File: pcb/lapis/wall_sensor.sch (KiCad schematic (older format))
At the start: 0 parts

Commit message: 基板修正途中　ソフト動作確認まで
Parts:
- added Q4: LTR-4206E, LED_THT:LED_D3.0mm_Horizontal_O1.27mm_Z2.0mm_IRBlack, symbol Device:Q_Photo_NPN
- added R5: 1k, Resistor_SMD:R_0201_0603Metric_Pad0.64x0.40mm_HandSolder, symbol Device:R
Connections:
- new net +3V3: Q4.1 (C)
- new net GND: R5.2
- new net WALLSENSOR_ADC: Q4.2 (E), R5.1
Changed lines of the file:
@@
 $Descr A4 11693 8268
 encoding utf-8
-Sheet 1 14
+Sheet 5 14
 Title ""
 Date ""
@@
 Comment4 ""
 $EndDescr
+$Comp
+L Device:Q_Photo_NPN Q4
+U 1 1 601D23CB
+P 5550 3850
+AR Path="/5FA82233/601D23CB" Ref="Q4"  Part="1"
+AR Path="/5FA821A9/601D23CB" Ref="Q1"  Part="1"
+AR Path="/5FA82246/601D23CB" Ref="Q3"  Part="1"
+AR Path="/5FA82203/601D23CB" Ref="Q2"  Part="1"
+F 0 "Q2" H 5740 3896 50  0000 L CNN
+F 1 "LTR-4206E" H 5740 3805 50  0000 L CNN
+F 2 "LED_THT:LED_D3.0mm_Horizontal_O1.27mm_Z2.0mm_IRBlack" H 5750 3950 50  0001 C CNN
+F 3 "~" H 5550 3850 50  0001 C CNN
+	1    5550 3850
+	1    0    0    -1
+$EndComp
+Wire Wire Line
+	5650 3650 5650 3400
+$Comp
+L power:GND #PWR0130
+U 1 1 601D7E50
+P 5650 4600
+AR Path="/5FA82233/601D7E50" Ref="#PWR0130"  Part="1"
+AR Path="/5FA821A9/601D7E50" Ref="#PWR0115"  Part="1"
+AR Path="/5FA82246/601D7E50" Ref="#PWR0128"  Part="1"
+AR Path="/5FA82203/601D7E50" Ref="#PWR0117"  Part="1"
+F 0 "#PWR0117" H 5650 4350 50  0001 C CNN
+F 1 "GND" H 5655 4427 50  0000 C CNN
+F 2 "" H 5650 4600 50  0001 C CNN
+F 3 "" H 5650 4600 50  0001 C CNN
+	1    5650 4600
+	1    0    0    -1
+$EndComp
+$Comp
+L Device:R R5
+U 1 1 601D7E56
+P 5650 4400
+AR Path="/5FA82233/601D7E56" Ref="R5"  Part="1"
+AR Path="/5FA821A9/601D7E56" Ref="R2"  Part="1"
+AR Path="/5FA82246/601D7E56" Ref="R4"  Part="1"
+AR Path="/5FA82203/601D7E56" Ref="R3"  Part="1"
+F 0 "R3" H 5720 4446 50  0000 L CNN
+F 1 "1k" H 5720 4355 50  0000 L CNN
+F 2 "Resistor_SMD:R_0201_0603Metric_Pad0.64x0.40mm_HandSolder" V 5580 4400 50  0001 C CNN
+F 3 "~" H 5650 4400 50  0001 C CNN
+	1    5650 4400
+	1    0    0    -1
+$EndComp
+Wire Wire Line
+	5650 4600 5650 4550
+Wire Wire Line
+	5650 4250 5650 4150
+Wire Wire Line
+	5650 4150 5850 4150
+Connection ~ 5650 4150
+Wire Wire Line
+	5650 4150 5650 4050
+Text HLabel 5850 4150 2    50   Output ~ 0
+WALLSENSOR_ADC
+$Comp
+L power:+3.3V #PWR?
+U 1 1 60612AF0
+P 5650 3400
+AR Path="/5FA81D59/60612AF0" Ref="#PWR?"  Part="1"
+AR Path="/5FA821A9/60612AF0" Ref="#PWR0114"  Part="1"
+AR Path="/5FA82203/60612AF0" Ref="#PWR0116"  Part="1"
+AR Path="/5FA82246/60612AF0" Ref="#PWR0125"  Part="1"
+AR Path="/5FA82233/60612AF0" Ref="#PWR0126"  Part="1"
+F 0 "#PWR0116" H 5650 3250 50  0001 C CNN
+F 1 "+3.3V" H 5665 3573 50  0000 C CNN
+F 2 "" H 5650 3400 50  0001 C CNN
+F 3 "" H 5650 3400 50  0001 C CNN
+	1    5650 3400
+	1    0    0    -1
+$EndComp
 $EndSCHEMATC

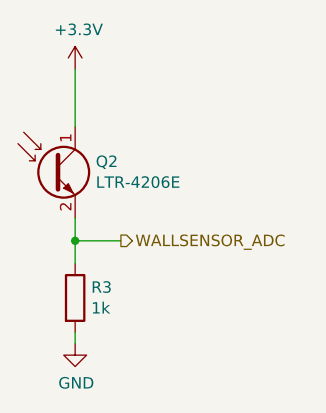
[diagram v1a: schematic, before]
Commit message: STM411失敗基板　STM484に変更し基板修正
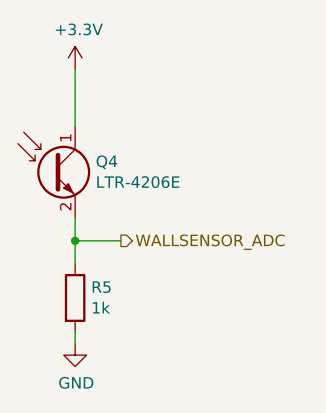
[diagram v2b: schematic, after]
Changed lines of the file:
@@
 AR Path="/5FA82246/601D23CB" Ref="Q3"  Part="1"
 AR Path="/5FA82203/601D23CB" Ref="Q2"  Part="1"
-F 0 "Q2" H 5740 3896 50  0000 L CNN
+F 0 "Q4" H 5740 3896 50  0000 L CNN
 F 1 "LTR-4206E" H 5740 3805 50  0000 L CNN
 F 2 "LED_THT:LED_D3.0mm_Horizontal_O1.27mm_Z2.0mm_IRBlack" H 5750 3950 50  0001 C CNN
@@
 AR Path="/5FA82246/601D7E50" Ref="#PWR0128"  Part="1"
 AR Path="/5FA82203/601D7E50" Ref="#PWR0117"  Part="1"
-F 0 "#PWR0117" H 5650 4350 50  0001 C CNN
+F 0 "#PWR0130" H 5650 4350 50  0001 C CNN
 F 1 "GND" H 5655 4427 50  0000 C CNN
 F 2 "" H 5650 4600 50  0001 C CNN
@@
 AR Path="/5FA82246/601D7E56" Ref="R4"  Part="1"
 AR Path="/5FA82203/601D7E56" Ref="R3"  Part="1"
-F 0 "R3" H 5720 4446 50  0000 L CNN
+F 0 "R5" H 5720 4446 50  0000 L CNN
 F 1 "1k" H 5720 4355 50  0000 L CNN
 F 2 "Resistor_SMD:R_0201_0603Metric_Pad0.64x0.40mm_HandSolder" V 5580 4400 50  0001 C CNN
@@
 AR Path="/5FA82246/60612AF0" Ref="#PWR0125"  Part="1"
 AR Path="/5FA82233/60612AF0" Ref="#PWR0126"  Part="1"
-F 0 "#PWR0116" H 5650 3250 50  0001 C CNN
+F 0 "#PWR0126" H 5650 3250 50  0001 C CNN
 F 1 "+3.3V" H 5665 3573 50  0000 C CNN
 F 2 "" H 5650 3400 50  0001 C CNN

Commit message: 信地旋回探索
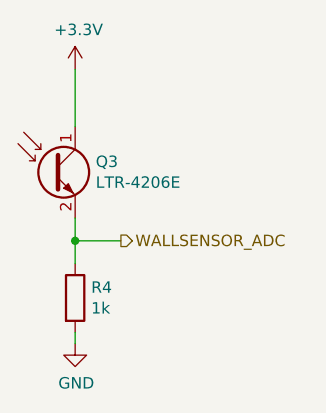
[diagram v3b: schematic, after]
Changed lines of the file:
@@
 $Descr A4 11693 8268
 encoding utf-8
-Sheet 5 14
+Sheet 10 15
 Title ""
 Date ""
@@
 AR Path="/5FA82246/601D23CB" Ref="Q3"  Part="1"
 AR Path="/5FA82203/601D23CB" Ref="Q2"  Part="1"
-F 0 "Q4" H 5740 3896 50  0000 L CNN
+F 0 "Q3" H 5740 3896 50  0000 L CNN
 F 1 "LTR-4206E" H 5740 3805 50  0000 L CNN
 F 2 "LED_THT:LED_D3.0mm_Horizontal_O1.27mm_Z2.0mm_IRBlack" H 5750 3950 50  0001 C CNN
@@
 AR Path="/5FA82246/601D7E50" Ref="#PWR0128"  Part="1"
 AR Path="/5FA82203/601D7E50" Ref="#PWR0117"  Part="1"
-F 0 "#PWR0130" H 5650 4350 50  0001 C CNN
+F 0 "#PWR0115" H 5650 4350 50  0001 C CNN
 F 1 "GND" H 5655 4427 50  0000 C CNN
 F 2 "" H 5650 4600 50  0001 C CNN
@@
 AR Path="/5FA82246/601D7E56" Ref="R4"  Part="1"
 AR Path="/5FA82203/601D7E56" Ref="R3"  Part="1"
-F 0 "R5" H 5720 4446 50  0000 L CNN
+F 0 "R4" H 5720 4446 50  0000 L CNN
 F 1 "1k" H 5720 4355 50  0000 L CNN
 F 2 "Resistor_SMD:R_0201_0603Metric_Pad0.64x0.40mm_HandSolder" V 5580 4400 50  0001 C CNN
@@
 AR Path="/5FA82246/60612AF0" Ref="#PWR0125"  Part="1"
 AR Path="/5FA82233/60612AF0" Ref="#PWR0126"  Part="1"
-F 0 "#PWR0126" H 5650 3250 50  0001 C CNN
+F 0 "#PWR0114" H 5650 3250 50  0001 C CNN
 F 1 "+3.3V" H 5665 3573 50  0000 C CNN
 F 2 "" H 5650 3400 50  0001 C CNN
